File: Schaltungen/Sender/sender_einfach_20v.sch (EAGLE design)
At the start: 9 parts, among them T2 BC327

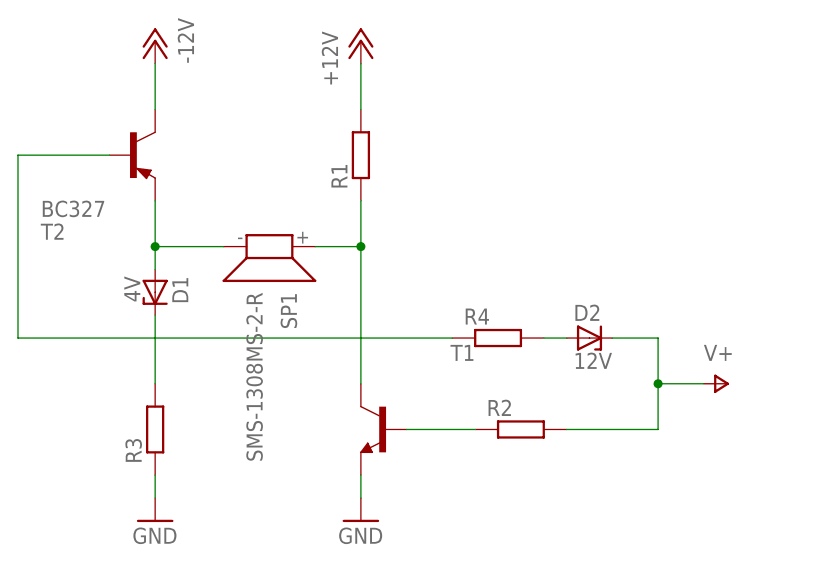
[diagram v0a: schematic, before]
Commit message: Sender-Schaltungen (12V und 20V) hinzugefügt. Programm zum öffnen: EAGLE (http://www.cadsoft.de/eagle-pcb-design-software/)
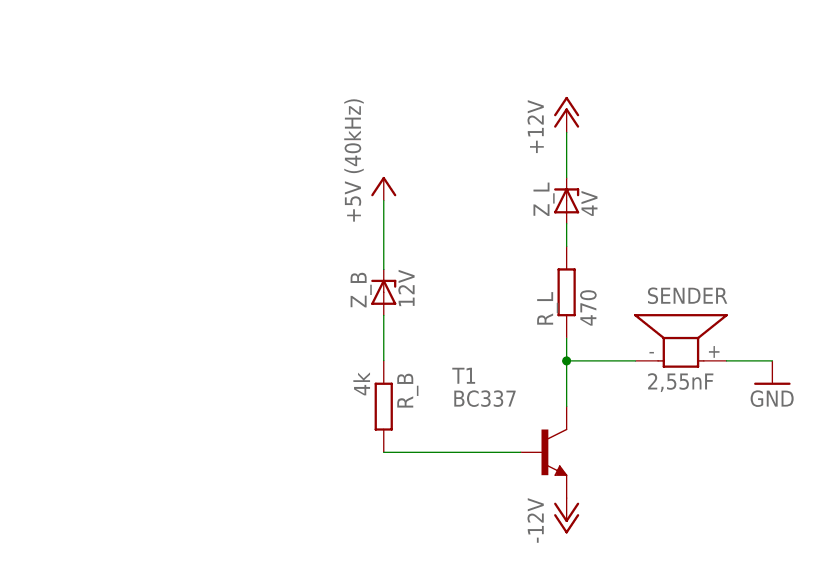
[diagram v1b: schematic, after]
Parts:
- removed D1: 4V, diode:ZENER-DIODEC1702-15
- removed D2: 12V, diode:ZENER-DIODEC1702-15
- removed R1, R2, R3, R4: (no value), resistor:R-EU_0204_7
- removed SP1: SMS-1308MS-2-R, speaker:SMS-1308MS-2-R
- removed T2: BC327, transistor-pnp:BC327
- added R_B: 4k, rcl:R-EU_0309/12
- added R_L: 470, rcl:R-EU_0309/12
- added SENDER: 2,55nF, buzzer:AL11P
- added Z_B: 12V, diode:ZENER-DIODEDO41Z10
- added Z_L: 4V, diode:ZENER-DIODEDO41Z10
- T1: value (none) -> BC337; device transistor:-NPN-TO92L -> transistor:BC337
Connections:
- removed net -12V: T2.C
- removed net N$3: D1.C, R3.2
- removed net N$4: D1.A, SP1.2, T2.E
- removed net N$5: D2.A, R4.2
- removed net N$6: R4.1, T2.B
- removed net V+: D2.C, R2.2
- new net +5V: Z_B.C
- new net PWM: R_B.1, Z_B.A
- new net R_L: R_L.1, SENDER.1, T1.C
- net +12V: now also Z_L.C; no longer R1.2
- net GND: now also SENDER.2; no longer R3.1
- net N$1: now also R_B.2, T1.B; no longer R1.1, SP1.1, T1.C
- net N$2: now also R_L.2, Z_L.A; no longer R2.1, T1.B
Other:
- moved on the sheet: T1
